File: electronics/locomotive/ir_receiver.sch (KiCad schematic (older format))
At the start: 0 parts

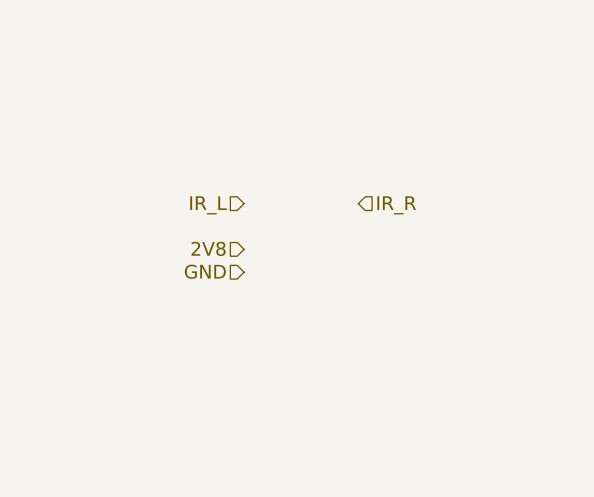
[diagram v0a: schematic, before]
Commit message: electronics: locomotive: Update schematics
Voltage regulator, TOF, IR receiver, voltage scaler, I2C control lines, power
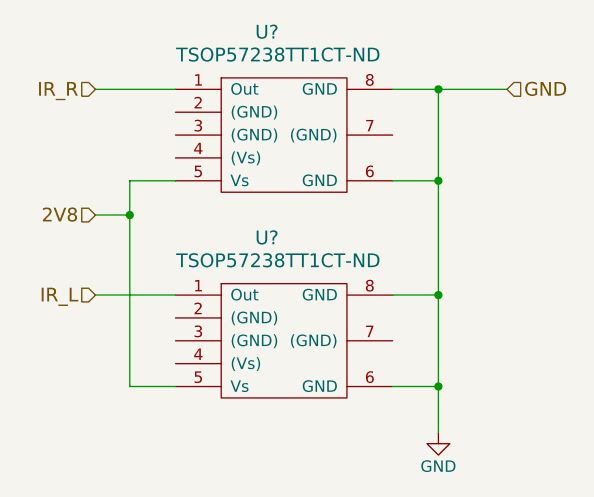
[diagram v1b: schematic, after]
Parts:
- added U? (x2): TSOP57238TT1CT-ND, symbol TSOP57238TT1CT-ND
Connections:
- net 2V8: now also U?.5 (Vs), U?.5 (Vs)
- net GND: now also U?.6 (GND), U?.6 (GND), U?.8 (GND), U?.8 (GND)
- net IR_L: now also U?.1 (Out)
- net IR_R: now also U?.1 (Out)
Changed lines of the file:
@@
 LIBS:valves
 LIBS:stm32
+LIBS:SPX3819
 LIBS:bcan
+LIBS:TSOP57238
 LIBS:locomotive-cache
 EELAYER 25 0
@@
 Comment4 ""
 $EndDescr
-Text HLabel 5300 4200 0    60   Input ~ 0
+Text HLabel 4650 4600 0    60   Input ~ 0
 IR_L
-Text HLabel 5800 4200 2    60   Input ~ 0
+Text HLabel 4650 3700 0    60   Input ~ 0
 IR_R
-Text HLabel 5300 4500 0    60   Input ~ 0
+Text HLabel 6450 3700 2    60   Input ~ 0
 GND
-Text HLabel 5300 4400 0    60   Input ~ 0
+Text HLabel 4650 4250 0    60   Input ~ 0
 2V8
+$Comp
+L TSOP57238TT1CT-ND U?
+U 1 1 58C5301A
+P 5400 3450
+F 0 "U?" H 5400 3450 60  0000 C CNN
+F 1 "TSOP57238TT1CT-ND" H 5450 3350 60  0000 C CNN
+F 2 "" H 5400 3450 60  0001 C CNN
+F 3 "" H 5400 3450 60  0001 C CNN
+	1    5400 3450
+	1    0    0    -1
+$EndComp
+$Comp
+L TSOP57238TT1CT-ND U?
+U 1 1 58C5305B
+P 5400 4350
+F 0 "U?" H 5400 4350 60  0000 C CNN
+F 1 "TSOP57238TT1CT-ND" H 5450 4250 60  0000 C CNN
+F 2 "" H 5400 4350 60  0001 C CNN
+F 3 "" H 5400 4350 60  0001 C CNN
+	1    5400 4350
+	1    0    0    -1
+$EndComp
+$Comp
+L GND #PWR041
+U 1 1 58C531F6
+P 6150 5200
+F 0 "#PWR041" H 6150 4950 50  0001 C CNN
+F 1 "GND" H 6150 5050 50  0000 C CNN
+F 2 "" H 6150 5200 50  0001 C CNN
+F 3 "" H 6150 5200 50  0001 C CNN
+	1    6150 5200
+	1    0    0    -1
+$EndComp
+Wire Wire Line
+	5950 3700 6450 3700
+Wire Wire Line
+	6150 3700 6150 5200
+Wire Wire Line
+	5950 5000 6150 5000
+Connection ~ 6150 5000
+Wire Wire Line
+	5950 4600 6150 4600
+Connection ~ 6150 4600
+Wire Wire Line
+	5950 4100 6150 4100
+Connection ~ 6150 4100
+Wire Wire Line
+	4650 3700 5000 3700
+Wire Wire Line
+	5000 4600 4650 4600
+Wire Wire Line
+	4650 4250 4800 4250
+Wire Wire Line
+	4800 4100 4800 5000
+Wire Wire Line
+	4800 4100 5000 4100
+Wire Wire Line
+	4800 5000 5000 5000
+Connection ~ 4800 4250
+Connection ~ 6150 3700
 $EndSCHEMATC
